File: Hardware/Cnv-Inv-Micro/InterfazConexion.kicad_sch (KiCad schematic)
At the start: 14 parts, among them J2 Screw_Terminal_01x07, J3 Screw_Terminal_01x03

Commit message: Normalizacion placa micros
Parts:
- removed J3: Screw_Terminal_01x03, TerminalBlock_Phoenix:TerminalBlock_Phoenix_MKDS-1,5-3-5.08_1x03_P5.08mm_Horizontal, symbol Connector:Screw_Terminal_01x03
- removed Micro_PwrBus_A1: Conn_01x02, Connector_Phoenix_MSTB:PhoenixContact_MSTBVA_2,5_2-G-5,08_1x02_P5.08mm_Vertical, symbol Connector_Generic:Conn_01x02
- removed Motor_Out_B1: Conn_01x03, Connector_Phoenix_MC_HighVoltage:PhoenixContact_MCV_1,5_3-G-5.08_1x03_P5.08mm_Vertical, symbol Connector_Generic:Conn_01x03
- removed Out_Motor1: Screw_Terminal_01x03, TerminalBlock_MetzConnect:TerminalBlock_MetzConnect_Type703_RT10N03HGLU_1x03_P9.52mm_Horizontal, symbol Connector:Screw_Terminal_01x03
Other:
- note added: "Conector de 12V para el conversor"
- note added: "Conector de 12V para el cooler"
- note added: "Conector de 12V para el inversor"
- note added: "Conectores externos"
- note added: "Conectores internos"
- note added: "Entrada de 12V en el frente, este alimenta los micros y toda la logica"
- note added: "Estos manejalos como te parezca conveniente"
- moved on the sheet: 12V_Pwr_In1, Cnv_Control_A2, Conv_PwrBus_A2, Cooler1, D17, Emg_Button1, Inv_PwrBus_A1, J2, R62, TermoSwitch1

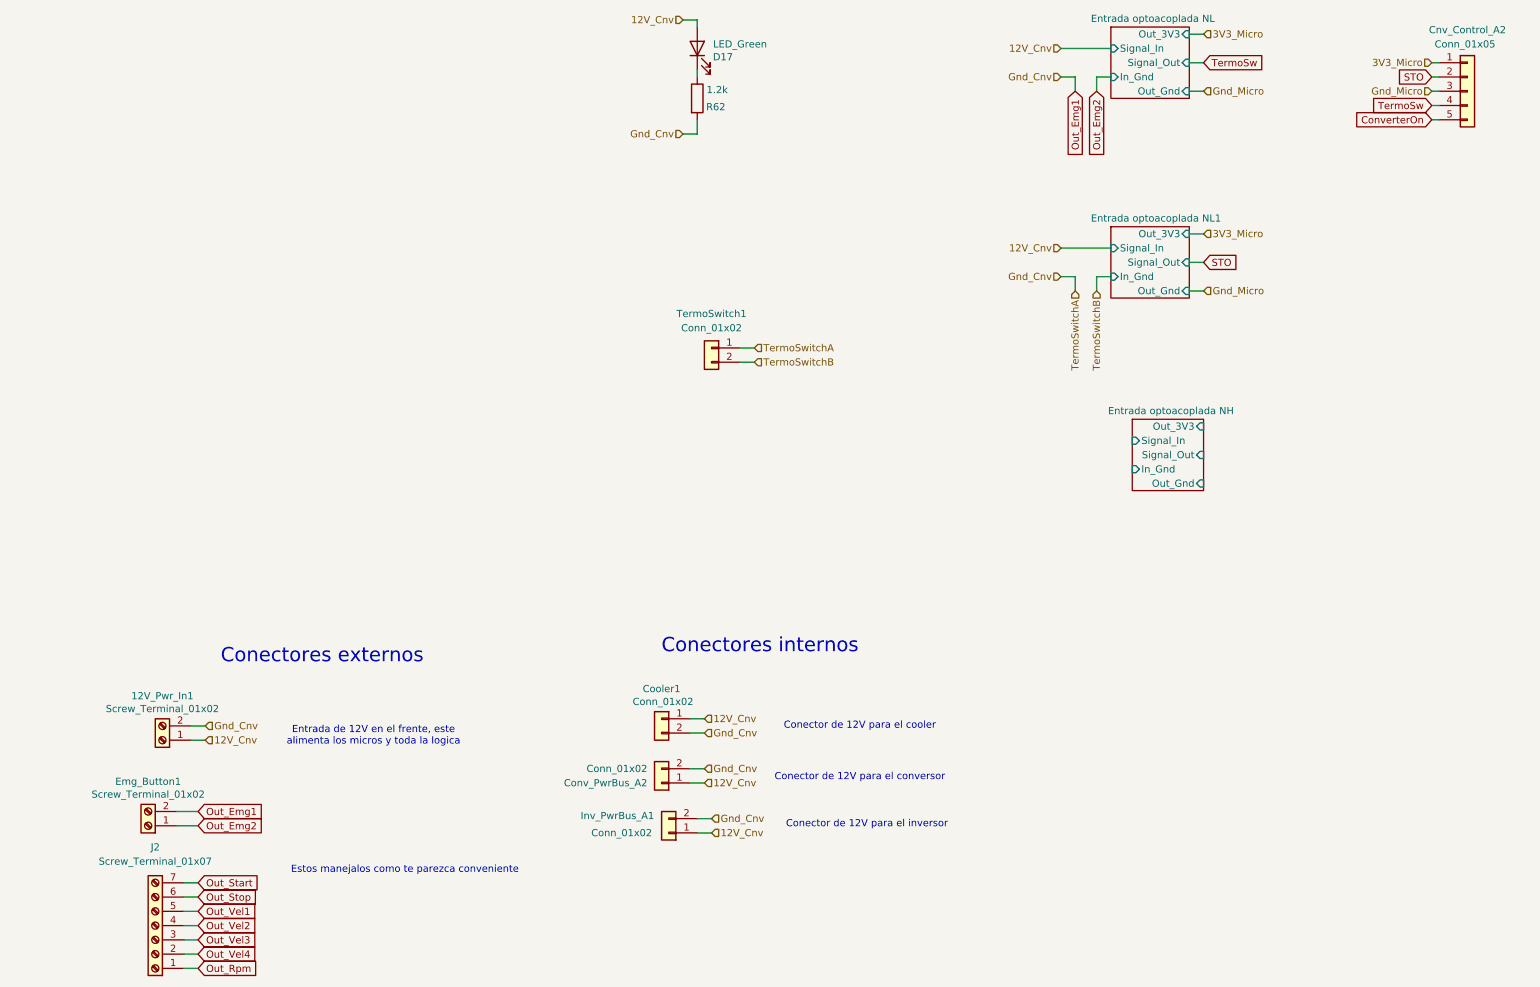
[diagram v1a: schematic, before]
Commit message: Avances en PCB conversor y inversor - Simulaciones de modulacion
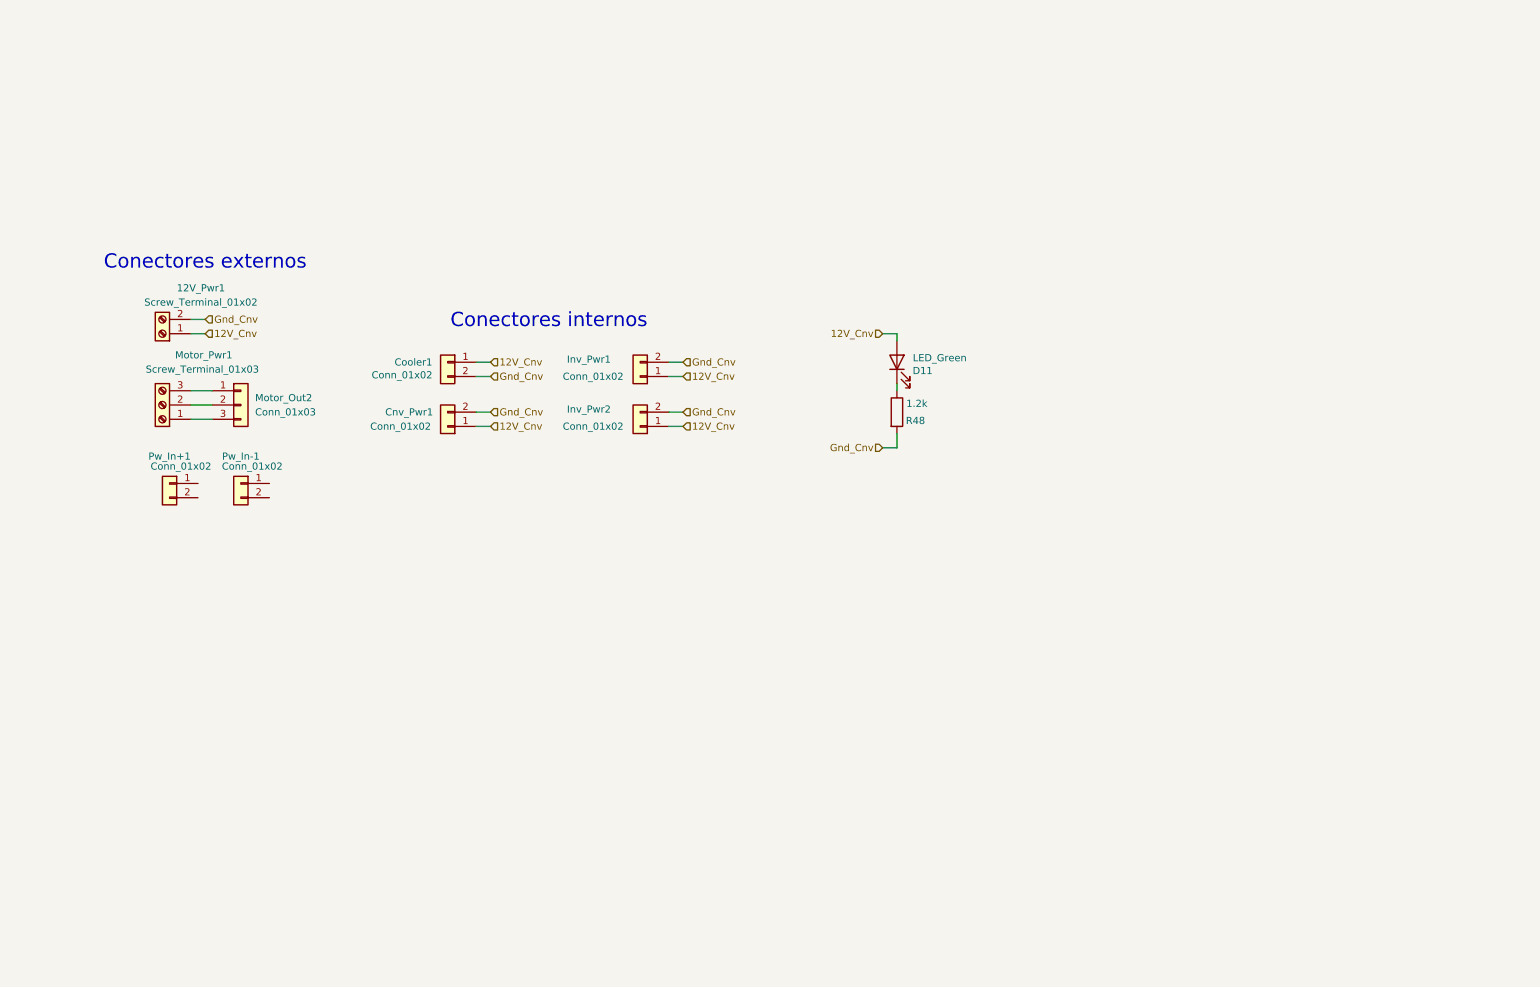
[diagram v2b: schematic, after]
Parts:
- removed Cnv_Control_A2: Conn_01x05, Connector_Molex:Molex_KK-254_AE-6410-05A_1x05_P2.54mm_Vertical, symbol Connector_Generic:Conn_01x05
- removed Emg_Button1: Screw_Terminal_01x02, TerminalBlock_Phoenix:TerminalBlock_Phoenix_MKDS-1,5-2_1x02_P5.00mm_Horizontal, symbol Connector:Screw_Terminal_01x02
- removed J2: Screw_Terminal_01x07, TerminalBlock_Phoenix:TerminalBlock_Phoenix_PT-1,5-7-5.0-H_1x07_P5.00mm_Horizontal, symbol Connector:Screw_Terminal_01x07
- removed TermoSwitch1: Conn_01x02, Connector_Molex:Molex_KK-254_AE-6410-02A_1x02_P2.54mm_Vertical, symbol Connector_Generic:Conn_01x02
- added Inv_Pwr2: Conn_01x02, Connector_Molex:Molex_KK-254_AE-6410-02A_1x02_P2.54mm_Vertical, symbol Connector_Generic:Conn_01x02
- added Motor_Out2: Conn_01x03, Connector_Phoenix_MC_HighVoltage:PhoenixContact_MCV_1,5_3-G-5.08_1x03_P5.08mm_Vertical, symbol Connector_Generic:Conn_01x03
- added Motor_Pwr1: Screw_Terminal_01x03, TerminalBlock_Dinkle:TerminalBlock_Dinkle_DT-55-B01X-03_P10.00mm, symbol Connector:Screw_Terminal_01x03
- added Pw_In+1, Pw_In-1: Conn_01x02, BananaSocket_THT:BananaSocket - 2P - 4mm, symbol Connector_Generic:Conn_01x02
- Cnv_Pwr1: renamed from Conv_PwrBus_A2; footprint Connector_Phoenix_MSTB:PhoenixContact_MSTBVA_2,5_2-G-5,08_1x02_P5.08mm_Vertical -> Connector_Molex:Molex_KK-254_AE-6410-02A_1x02_P2.54mm_Vertical
- Inv_Pwr1: renamed from Inv_PwrBus_A1; footprint Connector_Phoenix_MSTB:PhoenixContact_MSTBVA_2,5_2-G-5,08_1x02_P5.08mm_Vertical -> Connector_Molex:Molex_KK-254_AE-6410-02A_1x02_P2.54mm_Vertical
- R48: renamed from R62; footprint Resistor_SMD:R_0603_1608Metric_Pad0.98x0.95mm_HandSolder -> Resistor_THT:R_Axial_DIN0207_L6.3mm_D2.5mm_P10.16mm_Horizontal
- renumbered 12V_Pwr_In1 to 12V_Pwr1, D17 to D11
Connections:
- net 12V_Cnv: now also Inv_Pwr2.1 (Pin_1)
- net Out_Emg1 renamed Gnd_Cnv
- net Gnd_Cnv: now also Inv_Pwr2.2 (Pin_2)
- new net: Motor_Out2.3 (Pin_3), Motor_Pwr1.1 (Pin_1)
- new net: Motor_Out2.2 (Pin_2), Motor_Pwr1.2 (Pin_2)
- new net: Motor_Out2.1 (Pin_1), Motor_Pwr1.3 (Pin_3)
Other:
- removed sheet Entrada optoacoplada NH
- removed sheet Entrada optoacoplada NL
- removed sheet Entrada optoacoplada NL1
- note removed: "Conector de 12V para el conversor"
- note removed: "Conector de 12V para el cooler"
- note removed: "Conector de 12V para el inversor"
- note removed: "Entrada de 12V en el frente, este alimenta los micros y toda la logica"
- note removed: "Estos manejalos como te parezca conveniente"
- moved on the sheet: 12V_Pwr1, Cnv_Pwr1, Cooler1, D11, Inv_Pwr1, R48
